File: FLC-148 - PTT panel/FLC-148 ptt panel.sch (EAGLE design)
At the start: 6 parts

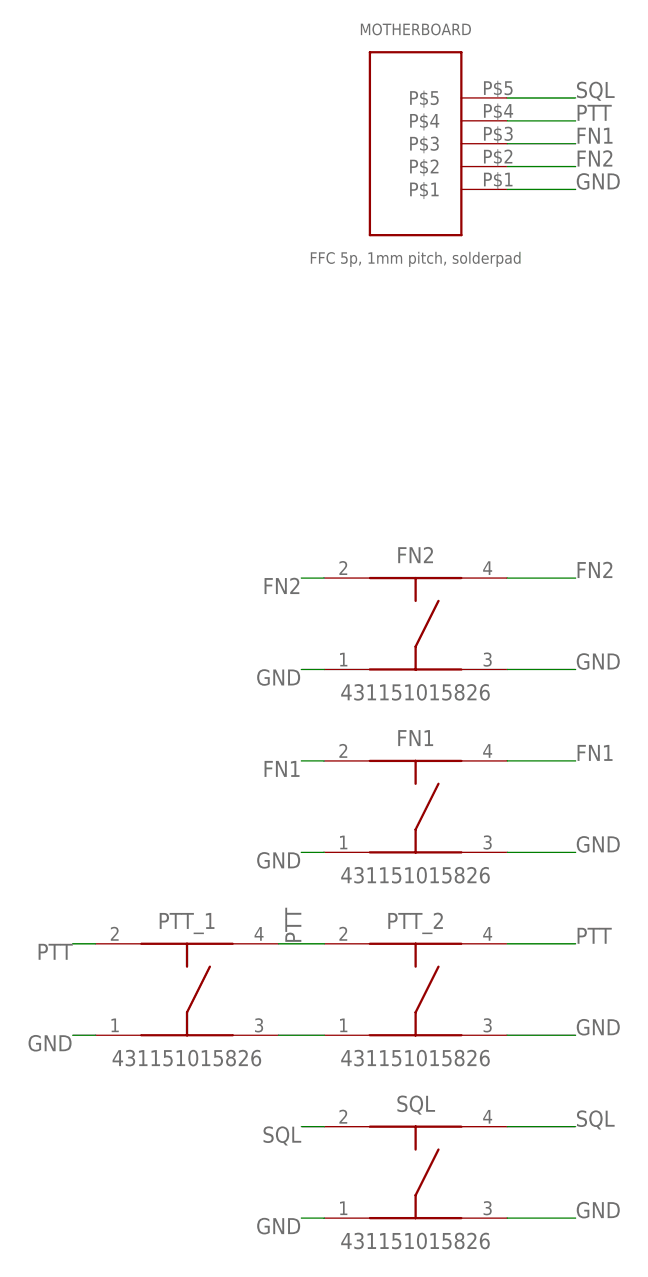
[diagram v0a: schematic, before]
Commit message: start of rev.2 board: - replaced existing tact pushbuttons with lower profile ones
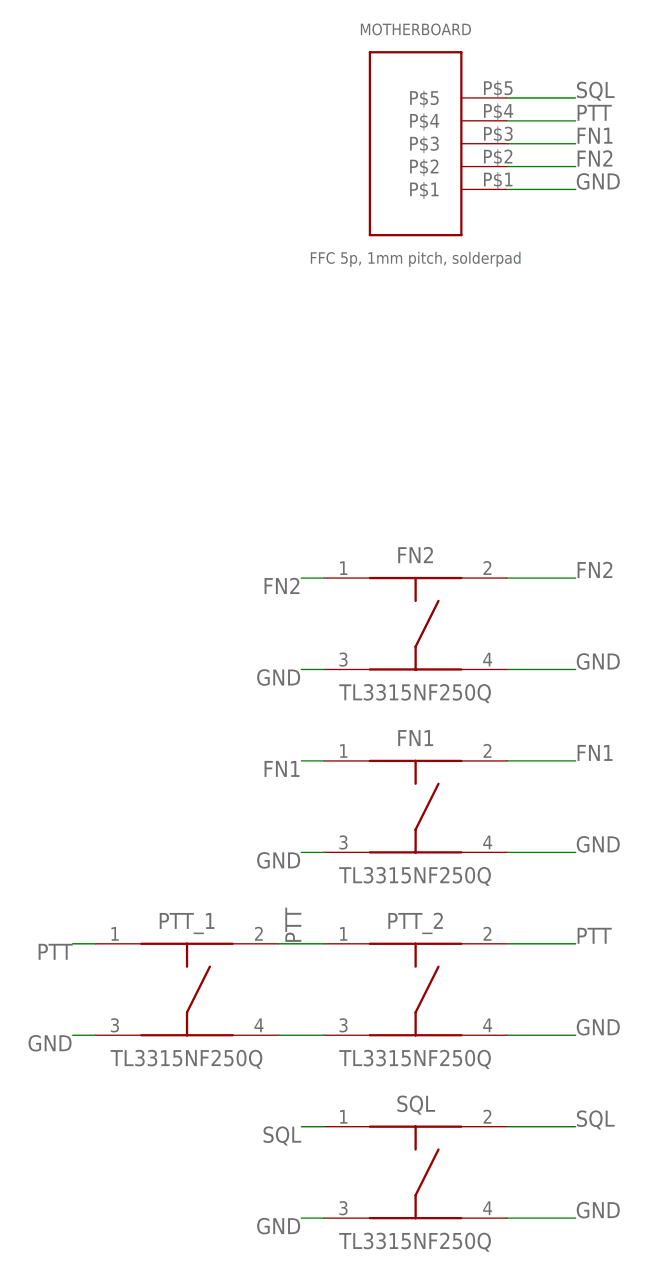
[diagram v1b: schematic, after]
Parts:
- FN1, FN2, PTT_1, PTT_2, SQL: value 431151015826 -> TL3315NF250Q; device 431151015826 WS-TASV SMT Tact Pushbutton:686605152001 -> TL3315-345930 SMT Tact Pushbutton:TL3315NF250Q
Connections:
- net FN1: now also FN1.1; no longer FN1.4
- net FN2: now also FN2.1; no longer FN2.4
- net GND: now also FN1.4, FN2.4, PTT_1.4, PTT_2.4, SQL.4; no longer FN1.1, FN2.1, PTT_1.1, PTT_2.1, SQL.1
- net PTT: now also PTT_1.1, PTT_2.1; no longer PTT_1.4, PTT_2.4
- net SQL: now also SQL.1; no longer SQL.4
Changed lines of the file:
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@@
 </classes>
 <parts>
-<part name="SQL" library="431151015826 WS-TASV SMT Tact Pushbutton" deviceset="686605152001" device="" value="431151015826"/>
-<part name="PTT_1" library="431151015826 WS-TASV SMT Tact Pushbutton" deviceset="686605152001" device="" value="431151015826"/>
-<part name="PTT_2" library="431151015826 WS-TASV SMT Tact Pushbutton" deviceset="686605152001" device="" value="431151015826"/>
-<part name="FN1" library="431151015826 WS-TASV SMT Tact Pushbutton" deviceset="686605152001" device="" value="431151015826"/>
-<part name="FN2" library="431151015826 WS-TASV SMT Tact Pushbutton" deviceset="686605152001" device="" value="431151015826"/>
+<part name="SQL" library="TL3315-345930 SMT Tact Pushbutton" deviceset="TL3315NF250Q" device="" value="TL3315NF250Q"/>
+<part name="PTT_1" library="TL3315-345930 SMT Tact Pushbutton" deviceset="TL3315NF250Q" device="" value="TL3315NF250Q"/>
+<part name="PTT_2" library="TL3315-345930 SMT Tact Pushbutton" deviceset="TL3315NF250Q" device="" value="TL3315NF250Q"/>
+<part name="FN1" library="TL3315-345930 SMT Tact Pushbutton" deviceset="TL3315NF250Q" device="" value="TL3315NF250Q"/>
+<part name="FN2" library="TL3315-345930 SMT Tact Pushbutton" deviceset="TL3315NF250Q" device="" value="TL3315NF250Q"/>
 <part name="MOTHERBOARD" library="FFC solder pad pitch 1mm 5p" deviceset="FFC_1MM_5P" device="" value="FFC 5p, 1mm pitch, solderpad"/>
 </parts>
@@
 <net name="GND" class="0">
 <segment>
-<pinref part="SQL" gate="G$1" pin="3"/>
+<pinref part="SQL" gate="G$1" pin="4"/>
 <wire x1="33.02" y1="10.16" x2="40.64" y2="10.16" width="0.1524" layer="91"/>
 <label x="40.64" y="10.16" size="1.778" layer="95"/>
 </segment>
 <segment>
-<pinref part="PTT_2" gate="G$1" pin="3"/>
+<pinref part="PTT_2" gate="G$1" pin="4"/>
 <wire x1="33.02" y1="30.48" x2="40.64" y2="30.48" width="0.1524" layer="91"/>
 <label x="40.64" y="30.48" size="1.778" layer="95"/>
 </segment>
 <segment>
-<pinref part="FN1" gate="G$1" pin="3"/>
+<pinref part="FN1" gate="G$1" pin="4"/>
 <wire x1="33.02" y1="50.8" x2="40.64" y2="50.8" width="0.1524" layer="91"/>
 <label x="40.64" y="50.8" size="1.778" layer="95"/>
 </segment>
 <segment>
-<pinref part="FN2" gate="G$1" pin="3"/>
+<pinref part="FN2" gate="G$1" pin="4"/>
 <wire x1="33.02" y1="71.12" x2="40.64" y2="71.12" width="0.1524" layer="91"/>
 <label x="40.64" y="71.12" size="1.778" layer="95"/>
 </segment>
 <segment>
-<pinref part="SQL" gate="G$1" pin="1"/>
+<pinref part="SQL" gate="G$1" pin="3"/>
 <wire x1="12.7" y1="10.16" x2="10.16" y2="10.16" width="0.1524" layer="91"/>
 <label x="10.16" y="10.16" size="1.778" layer="95" rot="R180"/>
 </segment>
 <segment>
-<pinref part="PTT_1" gate="G$1" pin="1"/>
+<pinref part="PTT_1" gate="G$1" pin="3"/>
 <wire x1="-12.7" y1="30.48" x2="-15.24" y2="30.48" width="0.1524" layer="91"/>
 <label x="-15.24" y="30.48" size="1.778" layer="95" rot="R180"/>
 </segment>
 <segment>
-<pinref part="PTT_1" gate="G$1" pin="3"/>
-<pinref part="PTT_2" gate="G$1" pin="1"/>
+<pinref part="PTT_1" gate="G$1" pin="4"/>
+<pinref part="PTT_2" gate="G$1" pin="3"/>
 <wire x1="12.7" y1="30.48" x2="7.62" y2="30.48" width="0.1524" layer="91"/>
 </segment>
 <segment>
-<pinref part="FN1" gate="G$1" pin="1"/>
+<pinref part="FN1" gate="G$1" pin="3"/>
 <wire x1="12.7" y1="50.8" x2="10.16" y2="50.8" width="0.1524" layer="91"/>
 <label x="10.16" y="50.8" size="1.778" layer="95" rot="R180"/>
 </segment>
 <segment>
-<pinref part="FN2" gate="G$1" pin="1"/>
+<pinref part="FN2" gate="G$1" pin="3"/>
 <wire x1="12.7" y1="71.12" x2="10.16" y2="71.12" width="0.1524" layer="91"/>
 <label x="10.16" y="71.12" size="1.778" layer="95" rot="R180"/>
@@
 <net name="PTT" class="1">
 <segment>
-<pinref part="PTT_2" gate="G$1" pin="4"/>
+<pinref part="PTT_2" gate="G$1" pin="2"/>
 <wire x1="33.02" y1="40.64" x2="40.64" y2="40.64" width="0.1524" layer="91"/>
 <label x="40.64" y="40.64" size="1.778" layer="95"/>
 </segment>
 <segment>
-<pinref part="PTT_1" gate="G$1" pin="2"/>
+<pinref part="PTT_1" gate="G$1" pin="1"/>
 <wire x1="-12.7" y1="40.64" x2="-15.24" y2="40.64" width="0.1524" layer="91"/>
 <label x="-15.24" y="40.64" size="1.778" layer="95" rot="R180"/>
 </segment>
 <segment>
-<pinref part="PTT_1" gate="G$1" pin="4"/>
-<pinref part="PTT_2" gate="G$1" pin="2"/>
+<pinref part="PTT_1" gate="G$1" pin="2"/>
+<pinref part="PTT_2" gate="G$1" pin="1"/>
 <wire x1="12.7" y1="40.64" x2="7.62" y2="40.64" width="0.1524" layer="91"/>
 <label x="10.16" y="40.64" size="1.778" layer="95" rot="R90"/>
@@
 <net name="FN1" class="0">
 <segment>
-<pinref part="FN1" gate="G$1" pin="4"/>
+<pinref part="FN1" gate="G$1" pin="2"/>
 <wire x1="33.02" y1="60.96" x2="40.64" y2="60.96" width="0.1524" layer="91"/>
 <label x="40.64" y="60.96" size="1.778" layer="95"/>
 </segment>
 <segment>
-<pinref part="FN1" gate="G$1" pin="2"/>
+<pinref part="FN1" gate="G$1" pin="1"/>
 <wire x1="12.7" y1="60.96" x2="10.16" y2="60.96" width="0.1524" layer="91"/>
 <label x="10.16" y="60.96" size="1.778" layer="95" rot="R180"/>
@@
 <net name="SQL" class="0">
 <segment>
-<pinref part="SQL" gate="G$1" pin="4"/>
+<pinref part="SQL" gate="G$1" pin="2"/>
 <wire x1="33.02" y1="20.32" x2="40.64" y2="20.32" width="0.1524" layer="91"/>
 <label x="40.64" y="20.32" size="1.778" layer="95"/>
 </segment>
 <segment>
-<pinref part="SQL" gate="G$1" pin="2"/>
+<pinref part="SQL" gate="G$1" pin="1"/>
 <wire x1="12.7" y1="20.32" x2="10.16" y2="20.32" width="0.1524" layer="91"/>
 <label x="10.16" y="20.32" size="1.778" layer="95" rot="R180"/>
@@
 <net name="FN2" class="0">
 <segment>
-<pinref part="FN2" gate="G$1" pin="4"/>
+<pinref part="FN2" gate="G$1" pin="2"/>
 <wire x1="33.02" y1="81.28" x2="40.64" y2="81.28" width="0.1524" layer="91"/>
 <label x="40.64" y="81.28" size="1.778" layer="95"/>
 </segment>
 <segment>
-<pinref part="FN2" gate="G$1" pin="2"/>
+<pinref part="FN2" gate="G$1" pin="1"/>
 <wire x1="12.7" y1="81.28" x2="10.16" y2="81.28" width="0.1524" layer="91"/>
 <label x="10.16" y="81.28" size="1.778" layer="95" rot="R180"/>
